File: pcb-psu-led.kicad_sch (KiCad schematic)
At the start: 1 part, among them T1 Talema 70000K

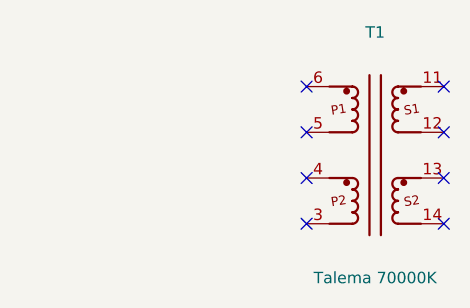
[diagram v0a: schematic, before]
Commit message: Add J1 and Talema primary series wiring
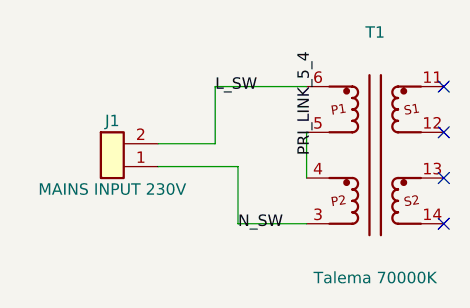
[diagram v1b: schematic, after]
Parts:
- added J1: MAINS INPUT 230V, symbol Connector_Generic:Conn_01x02
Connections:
- net N_SW: now reaches T1.3 (P2_END)
- net N_SW: now also J1.1 (Pin_1)
- net PRI_LINK_5_4: now reaches T1.4 (P2_START)
- net PRI_LINK_5_4: now also T1.5 (P1_END)
- net L_SW: now reaches T1.6 (P1_START)
- net L_SW: now also J1.2 (Pin_2)
- no-connect marks 8 -> 4
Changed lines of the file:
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@@
   (title_block
     (title "PCB PSU LED")
-    (rev "ECAD-01")
+    (rev "ECAD-02")
     (company "Custom Step-Down PSU 230 V to 100 V")
-    (comment 1 "T1 library and footprint integration checkpoint")
-  )
-  (no_connect
-    (at 93.98 93.98)
-  )
-  (no_connect
-    (at 93.98 99.06)
-  )
-  (no_connect
-    (at 93.98 104.14)
-  )
-  (no_connect
-    (at 93.98 109.22)
+    (comment 1 "J1 mains input and T1 primary series connection")
   )
   (no_connect
@@
     (at 109.22 109.22)
   )
+  (wire
+    (pts (xy 77.47 100.33) (xy 83.82 100.33))
+    (stroke
+      (width 0)
+      (type default)
+    )
+  )
+  (wire
+    (pts (xy 83.82 100.33) (xy 83.82 93.98))
+    (stroke
+      (width 0)
+      (type default)
+    )
+  )
+  (wire
+    (pts (xy 83.82 93.98) (xy 93.98 93.98))
+    (stroke
+      (width 0)
+      (type default)
+    )
+  )
+  (wire
+    (pts (xy 77.47 102.87) (xy 86.36 102.87))
+    (stroke
+      (width 0)
+      (type default)
+    )
+  )
+  (wire
+    (pts (xy 86.36 102.87) (xy 86.36 109.22))
+    (stroke
+      (width 0)
+      (type default)
+    )
+  )
+  (wire
+    (pts (xy 86.36 109.22) (xy 93.98 109.22))
+    (stroke
+      (width 0)
+      (type default)
+    )
+  )
+  (wire
+    (pts (xy 93.98 99.06) (xy 93.98 104.14))
+    (stroke
+      (width 0)
+      (type default)
+    )
+  )
+  (label "L_SW"
+    (at 83.82 93.98 0)
+    (effects
+      (font (size 1.27 1.27))
+    )
+  )
+  (label "N_SW"
+    (at 86.36 109.22 0)
+    (effects
+      (font (size 1.27 1.27))
+    )
+  )
+  (label "PRI_LINK_5_4"
+    (at 93.98 101.6 90)
+    (effects
+      (font (size 1.27 1.27))
+    )
+  )
   (symbol
+    (lib_id "Connector_Generic:Conn_01x02")
+    (at 72.39 101.6 0)
+    (unit 1)
+    (exclude_from_sim no)
+    (in_bom yes)
+    (on_board yes)
+    (dnp no)
+    (fields_autoplaced yes)
+    (property "Reference" "J1"
+      (at 72.39 97.79 0)
+      (effects
+        (font (size 1.27 1.27))
+      )
+    )
+    (property "Value" "MAINS INPUT 230V"
+      (at 72.39 105.41 0)
+      (effects
+        (font (size 1.27 1.27))
+      )
+    )
+    (property "Footprint" ""
+      (at 72.39 101.6 0)
+      (effects
+        (font (size 1.27 1.27))
+        (hide yes)
+      )
+    )
+    (property "Datasheet" "~"
+      (at 72.39 101.6 0)
+      (effects
+        (font (size 1.27 1.27))
+        (hide yes)
+      )
+    )
+    (property "Description" "2-pin mains input from NKK switch; exact Phoenix Contact part pending"
+      (at 72.39 101.6 0)
+      (effects
+        (font (size 1.27 1.27))
+        (hide yes)
+      )
+    )
+    (property "Manufacturer" "Phoenix Contact"
+      (at 72.39 101.6 0)
+      (effects
+        (font (size 1.27 1.27))
+        (hide yes)
+      )
+    )
+    (property "MPN" "TBD"
+      (at 72.39 101.6 0)
+      (effects
+        (font (size 1.27 1.27))
+        (hide yes)
+      )
+    )
+    (pin "1"
+    )
+    (pin "2"
+    )
+    (instances
+      (project "pcb-psu-led"
+        (path "/a08e89e5-29a6-4ee5-b521-7a214388ab56"
+          (reference "J1")
+          (unit 1)
+        )
+      )
+    )
+  )
+  (symbol

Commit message: Migrate J1 to local project symbol
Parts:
- J1: symbol Connector_Generic:Conn_01x02 -> PSU_LED:Conn_01x02
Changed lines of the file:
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@@
   (title_block
     (title "PCB PSU LED")
-    (rev "ECAD-02")
+    (rev "ECAD-03")
     (company "Custom Step-Down PSU 230 V to 100 V")
-    (comment 1 "J1 mains input and T1 primary series connection")
+    (comment 1 "J1 migrated to local project symbol library")
   )
   (no_connect
@@
   )
   (symbol
-    (lib_id "Connector_Generic:Conn_01x02")
+    (lib_id "PSU_LED:Conn_01x02")
     (at 72.39 101.6 0)
     (unit 1)

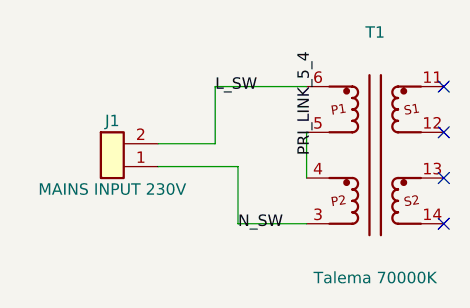
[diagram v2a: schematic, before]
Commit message: Mirror J1 to restore pin 1 L and pin 2 N
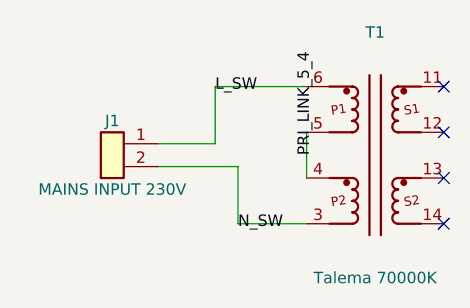
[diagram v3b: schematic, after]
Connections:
- net L_SW: now also J1.1 (Pin_1); no longer J1.2 (Pin_2)
- net N_SW: now also J1.2 (Pin_2); no longer J1.1 (Pin_1)
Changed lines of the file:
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@@
   (title_block
     (title "PCB PSU LED")
-    (rev "ECAD-03")
+    (rev "ECAD-04")
     (company "Custom Step-Down PSU 230 V to 100 V")
-    (comment 1 "J1 migrated to local project symbol library")
+    (comment 1 "J1 pin order aligned: pin 1 L_SW, pin 2 N_SW")
   )
   (no_connect
@@
     (lib_id "PSU_LED:Conn_01x02")
     (at 72.39 101.6 0)
+    (mirror x)
     (unit 1)
     (exclude_from_sim no)
